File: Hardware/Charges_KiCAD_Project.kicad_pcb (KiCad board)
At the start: 4 copper layers, 80 x 93.2 mm, 81 parts, among them J1 Terminal Block, J2 Terminal Block, J3 DB37_Male_MountingHoles, J4 10118192-0001LF, Q1 SI7232DN-T1-GE3, Q2 SI7232DN-T1-GE3, SW1 MCU Reset, U1 MS5607-02BA, U2 STM32L562VET6Q, U3 LP38692MPX-ADJ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

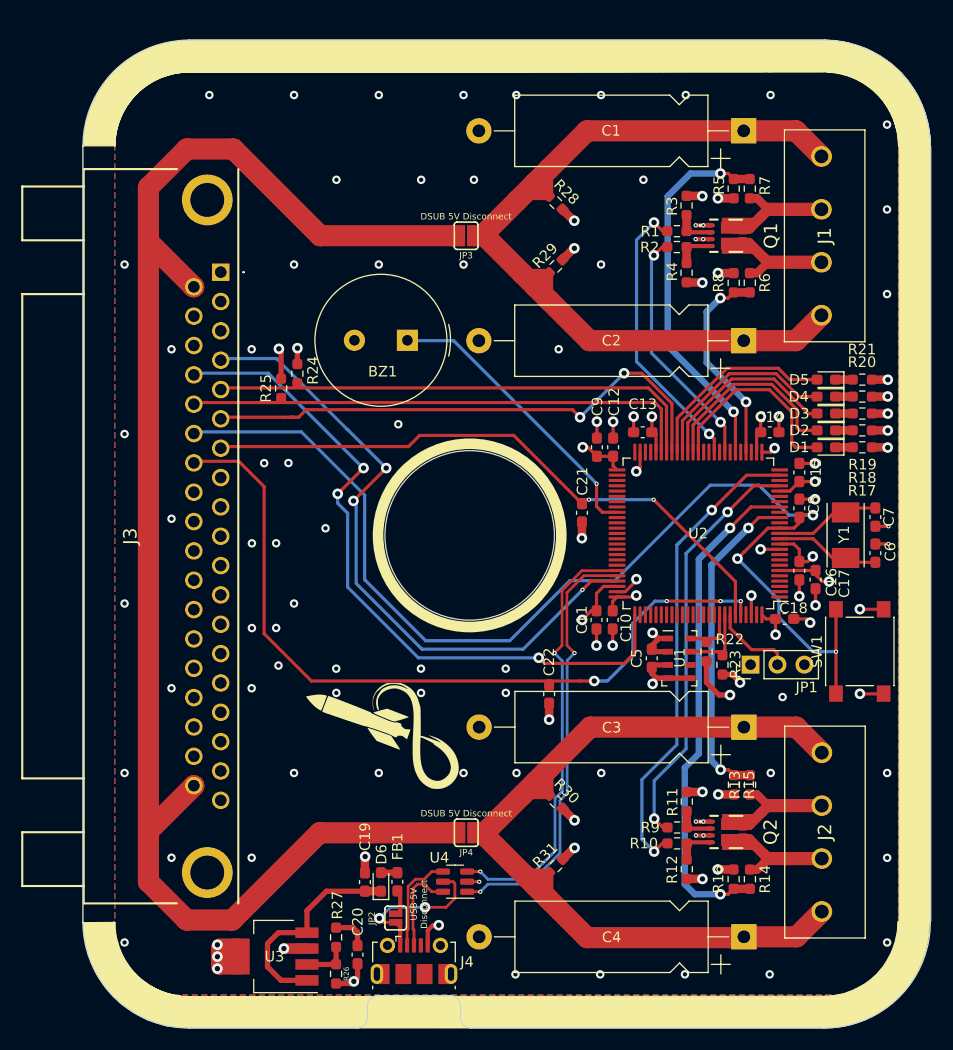
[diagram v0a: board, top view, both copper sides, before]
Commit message: Updated hole location
Hole was moved 2mm to the left to fit tolerances
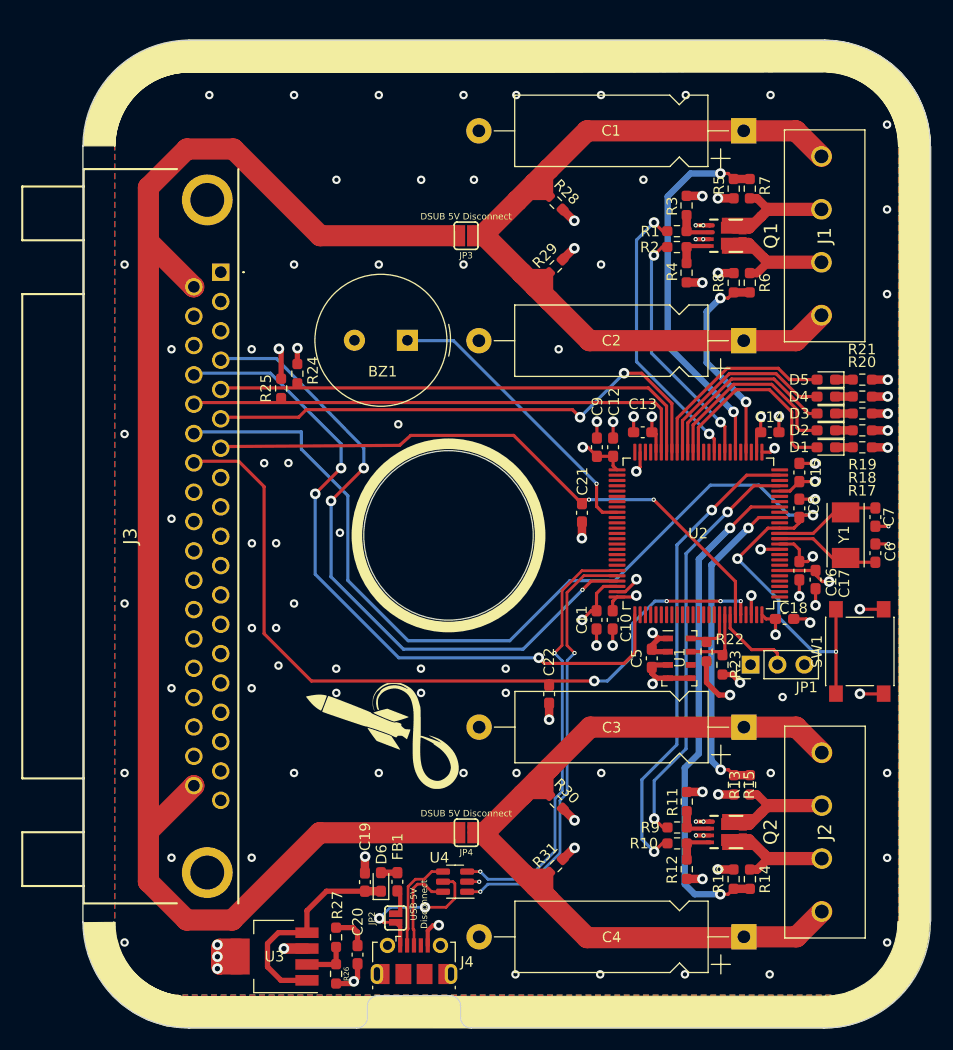
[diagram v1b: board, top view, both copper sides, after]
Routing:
- net /37 Pin DSUB/SWDIO: track 61.6 -> 63.0 mm
- net /37 Pin DSUB/SWCLK: track 66.5 -> 67.6 mm
- net GND: track 93.9 -> 93.1 mm
- net /37 Pin DSUB/NRST: track 109.9 -> 110.5 mm
- net +3V3: track 56.0 -> 55.5 mm
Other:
- outline, holes or cut-outs redrawn

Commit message: Corrected edge cuts, aligned silkscreen border, aligned all components, aligned grid/drill origin, aligned center hole
Some traces need to be corrected around the center hole
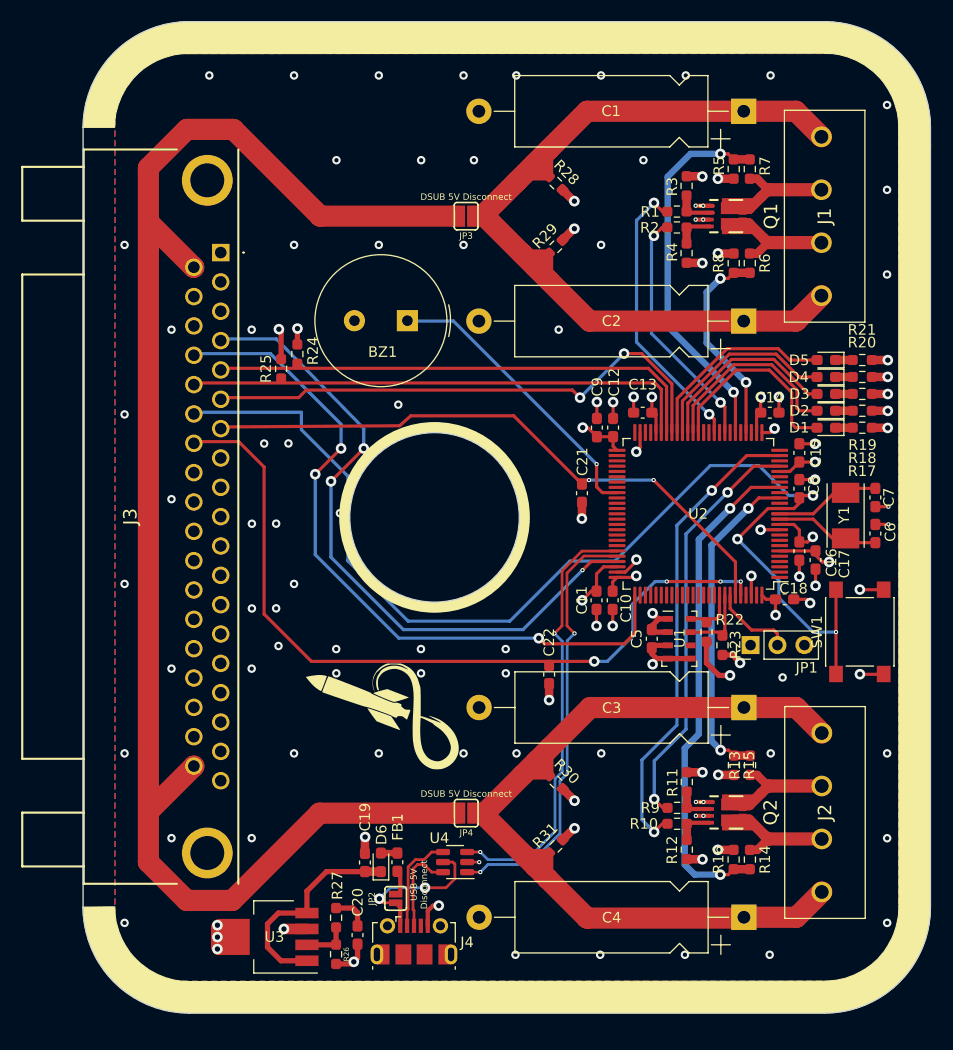
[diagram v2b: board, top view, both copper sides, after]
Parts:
- added G***: LOGO, RDT_Graphics:RDT_Logo, B.Cu at (100.6, 96.8)
- moved C20 1.85 mm to (105.9, 136.2)
- moved FB1 1.85 mm to (109.7, 129.4)
- moved R12 1.85 mm to (137.0, 128.2)
- moved R16 1.85 mm to (141.4, 129.1)
- moved R26 1.85 mm to (103.9, 138.0)
- moved C10 1.85 mm to (130.0, 104.6)
- moved C11 1.85 mm to (128.5, 104.6)
- moved C12 1.85 mm to (130.0, 88.3)
- moved C13 1.85 mm to (132.8, 86.9)
- moved C14 1.85 mm to (144.8, 86.9)
- moved C18 1.85 mm to (146.2, 104.5)
- moved C2 1.85 mm to (142.4, 78.3)
- moved C21 1.85 mm to (127.1, 94.5)
- moved C3 1.85 mm to (142.4, 114.7)
- moved C5 1.85 mm to (133.7, 108.3)
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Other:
- board size 80 x 93.2 mm -> 80 x 93.6 mm
